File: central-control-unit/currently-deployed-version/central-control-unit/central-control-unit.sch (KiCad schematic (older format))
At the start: 24 parts, among them J4 1x2_screw_term_block, P1 1x3_pin_header, P2 1x3_pin_header, P26 1x4_pin_socket, P28 1x2_pin_header, P3 1x3_pin_header, P30 1x2_pin_header, Q56 YJD20N06A, Q57 YJD20N06A, U8 MCP23S17

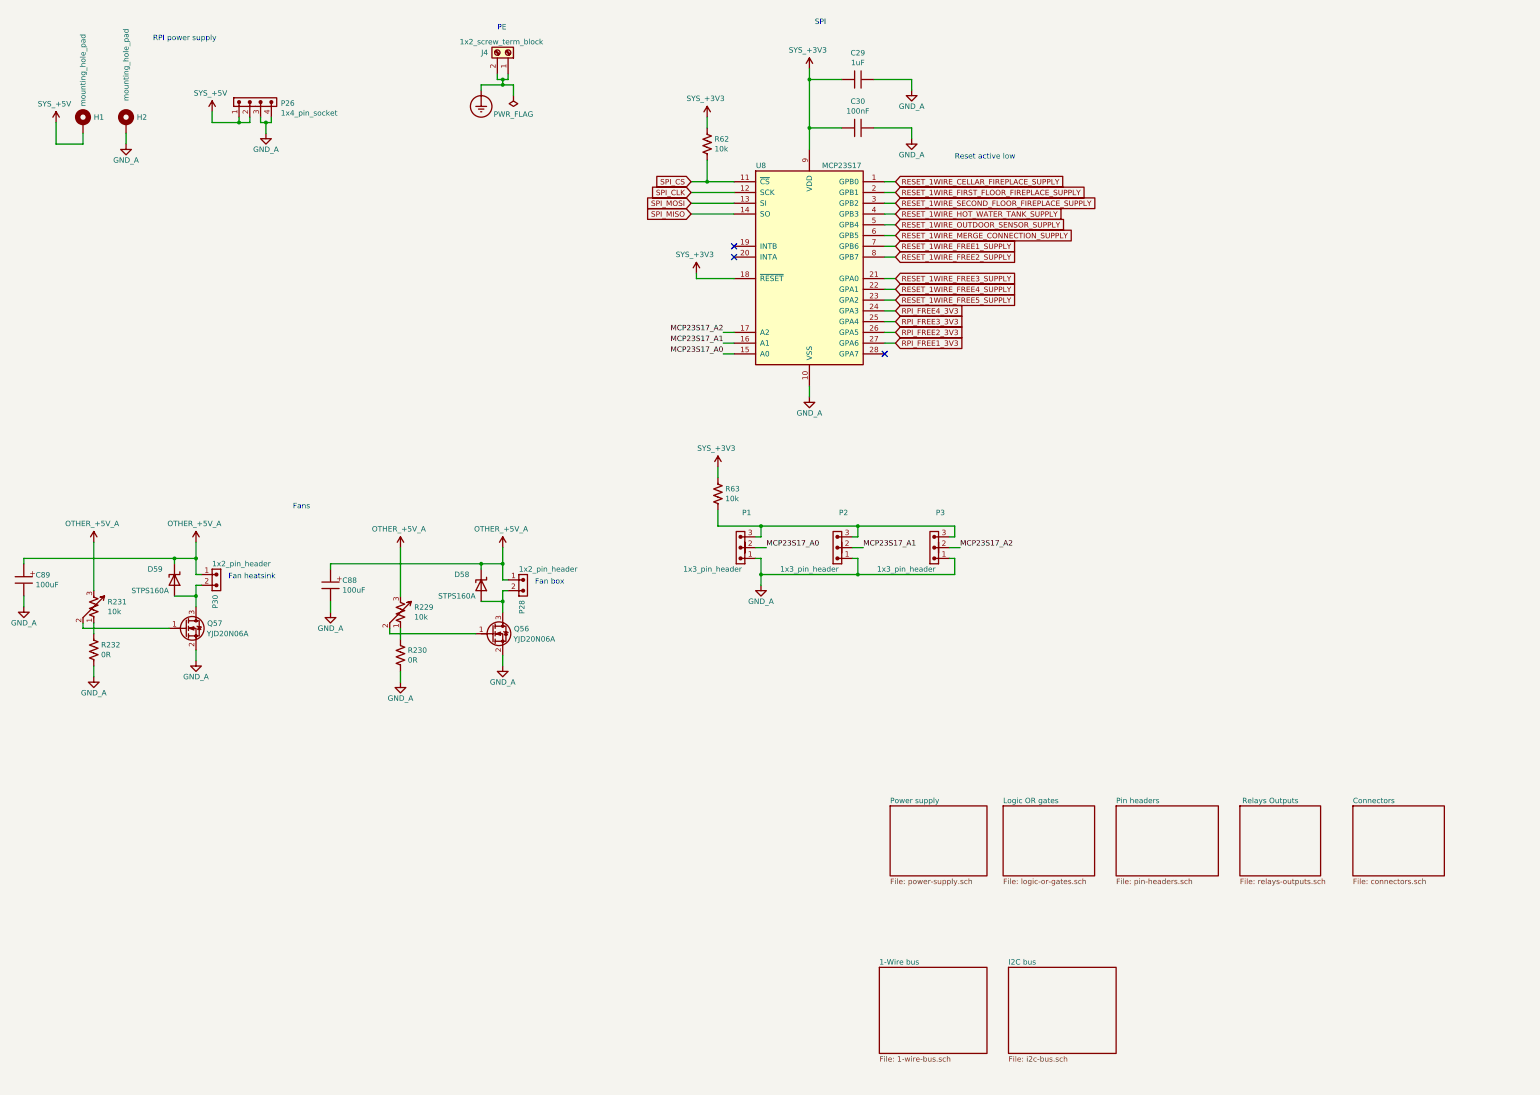
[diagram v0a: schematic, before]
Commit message: Adding of information about projects.
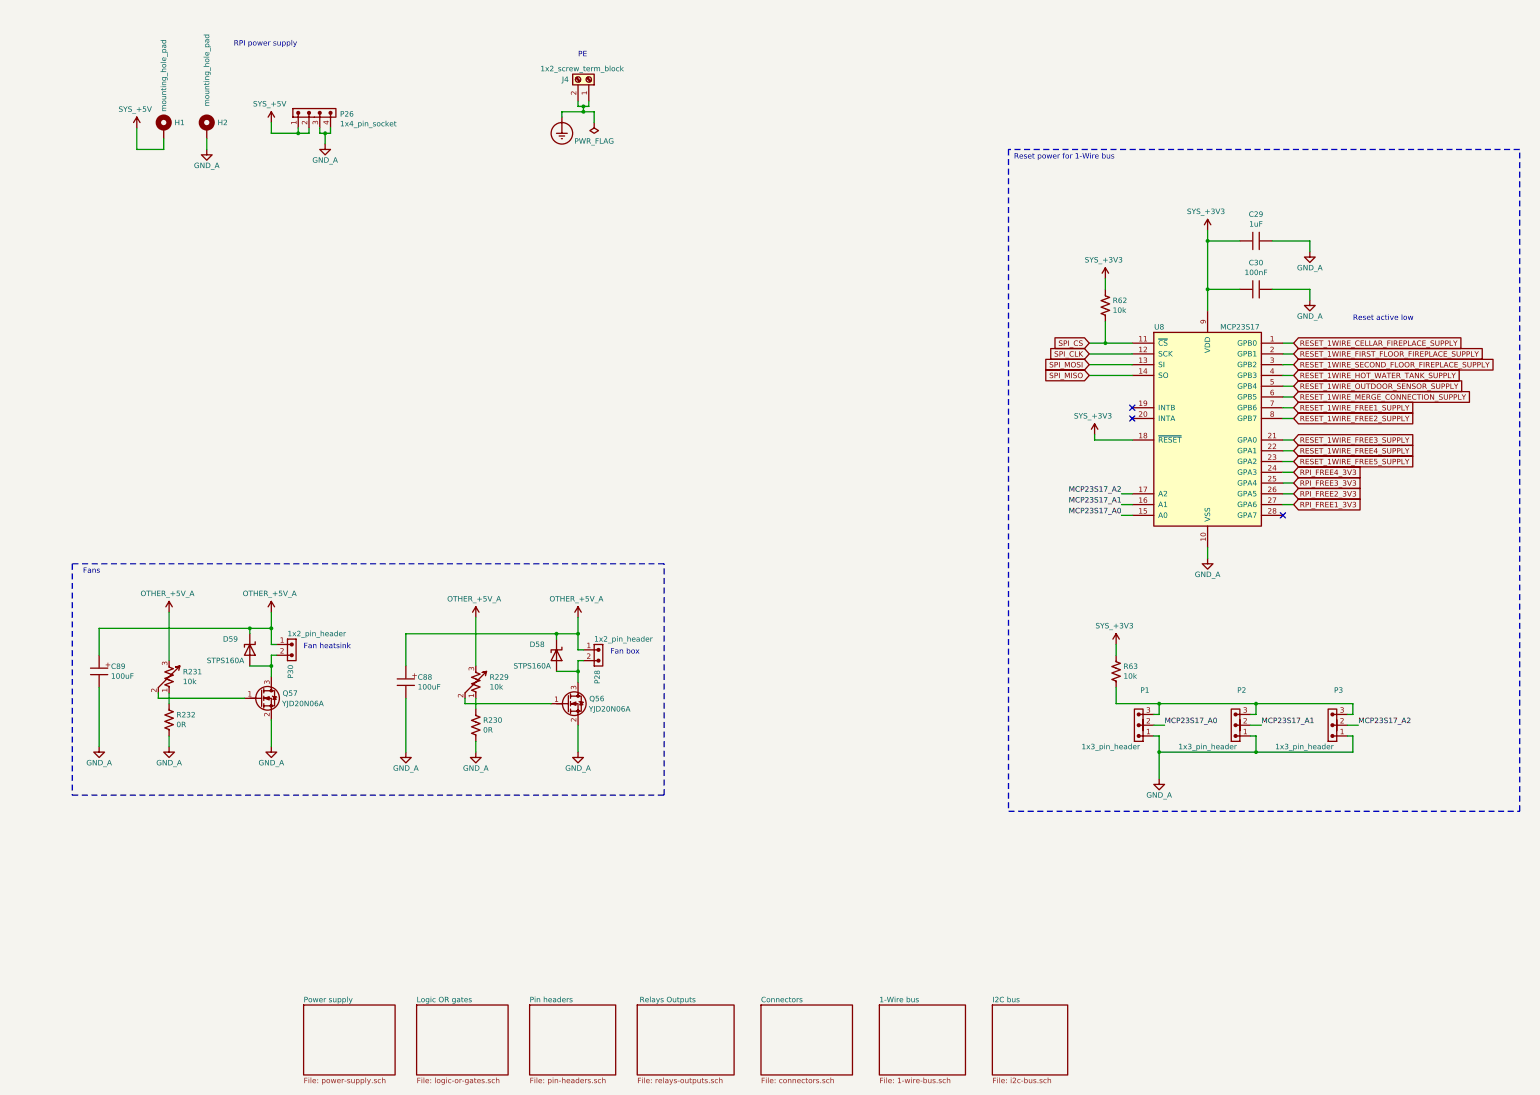
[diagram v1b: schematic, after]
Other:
- note added: "Reset power for 1-Wire bus"
- note removed: "SPI"
- moved on the sheet: C29, C30, C88, C89, D58, D59, H1, H2, J4, P1, P2, P26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
